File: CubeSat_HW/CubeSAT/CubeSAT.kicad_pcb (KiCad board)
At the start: 2 copper layers, 85 x 56 mm, 13 parts, among them J1 Conn_02x06_Odd_Even, J2 Conn_02x04_Odd_Even, J4 Conn_01x08_Pin, J5 Conn_01x06_Pin

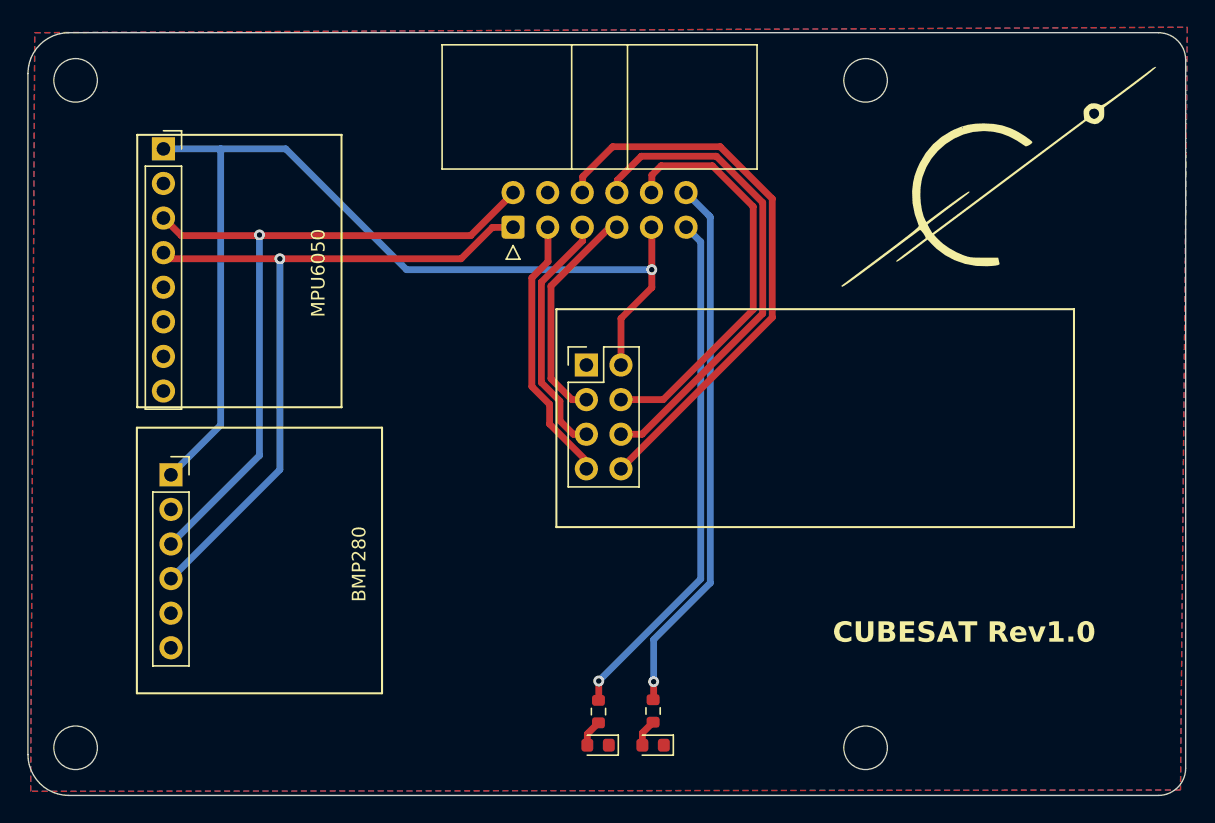
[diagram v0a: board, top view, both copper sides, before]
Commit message: Added version 2 of the PCB
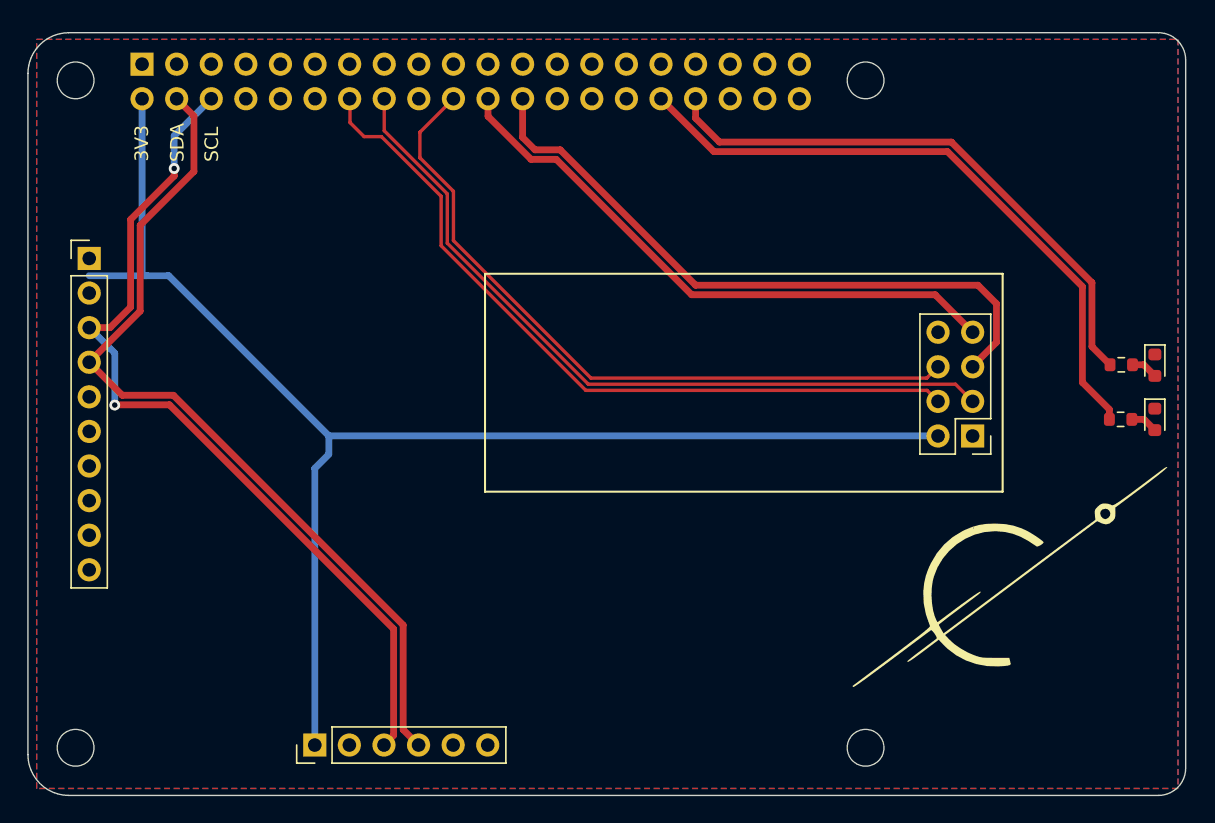
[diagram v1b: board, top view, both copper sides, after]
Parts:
- H1, H2, H3, H4: footprint MountingHole:MountingHole_3.2mm_M3 -> MountingHole:MountingHole_2.7mm
- J1: value Conn_02x06_Odd_Even -> Conn_01x10_Pin; footprint Connector_IDC:IDC-Header_2x06_P2.54mm_Horizontal -> Connector_PinHeader_2.54mm:PinHeader_1x10_P2.54mm_Vertical
- J4: value Conn_01x08_Pin -> Conn_02x20_Odd_Even; footprint Connector_PinSocket_2.54mm:PinSocket_1x08_P2.54mm_Vertical -> Connector_PinHeader_2.54mm:PinHeader_2x20_P2.54mm_Vertical; moved to B.Cu
- J5: footprint Connector_PinSocket_2.54mm:PinSocket_1x06_P2.54mm_Vertical -> Connector_PinHeader_2.54mm:PinHeader_1x06_P2.54mm_Vertical
- moved D1 49.5 mm to (262.7, 84.4), turned to -90 degrees
- moved R1 46.1 mm to (260.3, 84.4), turned to 0 degrees
- moved D2 43.9 mm to (262.7, 88.4), turned to -90 degrees
- moved R2 40.5 mm to (260.2, 88.4), turned to 0 degrees
- moved J1 31.2 mm to (184.5, 76.6), turned to 0 degrees
- moved G*** 29.4 mm to (252.1, 101.4)
- moved J2 28.8 mm to (249.4, 89.6), turned to 180 degrees
- moved J5 22.5 mm to (201.1, 112.3), turned to 90 degrees
- moved J4 6.42 mm to (188.4, 62.3), turned to -90 degrees
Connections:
- J1 pad 1: /SDA -> +3.3V
- J1 pad 10: /CSN -> unconnected-(J1-Pin_10-Pad10)
- J1 pad 2: /SCL -> GND
- J1 pad 3: /MISO -> /SCL
- J1 pad 4: GND -> /SDA
- J1 pad 5: /SCK -> unconnected-(J1-Pin_5-Pad5)
- J1 pad 6: /IRQ -> unconnected-(J1-Pin_6-Pad6)
- J1 pad 7: /CE -> unconnected-(J1-Pin_7-Pad7)
- J1 pad 8: /MOSI -> unconnected-(J1-Pin_8-Pad8)
- J1 pad 9: +3.3V -> unconnected-(J1-Pin_9-Pad9)
- J2 pad 8: /IRQ -> unconnected-(J2-Pin_8-Pad8)
- J4 pad 1: +3.3V -> unconnected-(J4-Pin_1-Pad1)
- J4 pad 2: GND -> +3.3V
- J4 pad 3: /SCL -> unconnected-(J4-Pin_3-Pad3)
- J4 pad 5: unconnected-(J4-Pin_5-Pad5) -> GND
- J4 pad 6: unconnected-(J4-Pin_6-Pad6) -> /SCL
- J4 pad 7: unconnected-(J4-Pin_7-Pad7) -> /TXD
- J4 pad 8: unconnected-(J4-Pin_8-Pad8) -> /GPIO4
- R1 pad 1: Net-(J1-Pin_11) -> /LED_1
- R2 pad 1: Net-(J1-Pin_12) -> /LED_2
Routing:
- net /LED_2: track 0.00 -> 47.2 mm
- net /LED_1: track 0.00 -> 42.1 mm
- net /IRQ: track 42.0 -> 0.00 mm
- net Net-(J1-Pin_12): track 39.7 -> 0.00 mm, vias 1 -> 0
- net /CE: track 16.7 -> 55.9 mm
- net Net-(J1-Pin_11): track 38.3 -> 0.00 mm, vias 1 -> 0
- net /SCK: track 18.4 -> 48.2 mm
- net +3.3V: track 76.0 -> 103.7 mm, vias 1 -> 0
- net /CSN: track 30.3 -> 55.5 mm
- net /MISO: track 19.9 -> 43.6 mm
- net /MOSI: track 36.0 -> 52.6 mm
- net /SCL: track 53.0 -> 64.0 mm, vias 1 -> 2
- net /SDA: track 53.6 -> 63.4 mm, vias 1 -> 0
- net GND: track 0.00 -> 0.57 mm
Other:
- board text added: "3V3"
- board text added: "CUBESAT Rev2.0"
- board text added: "SCL"
- board text added: "SDA"
- board text removed: "BMP280"
- board text removed: "CUBESAT Rev1.0"
- board text removed: "MPU6050"

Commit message: feat: Added Power and Com PCB
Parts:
- removed G***: LOGO, Logo:Logo
- removed J5: Conn_01x06_Pin, Connector_PinHeader_2.54mm:PinHeader_1x06_P2.54mm_Vertical
- added D3: G_LED, LED_SMD:LED_0603_1608Metric, F.Cu at (186.9, 93.0)
- added D4: G_LED, LED_SMD:LED_0603_1608Metric, F.Cu at (186.9, 88.0)
- added D5: G_LED, LED_SMD:LED_0603_1608Metric, F.Cu at (186.9, 98.0)
- added R3: 100R, Resistor_SMD:R_0603_1608Metric, F.Cu at (189.3, 93.0)
- added R4: 100R, Resistor_SMD:R_0603_1608Metric, F.Cu at (189.3, 88.0)
- added R5: 100R, Resistor_SMD:R_0603_1608Metric, F.Cu at (189.3, 98.0)
- moved D1 76.1 mm to (186.9, 78.0), turned to 90 degrees
- moved D2 76.0 mm to (186.9, 83.0), turned to 90 degrees
- moved R1 71.3 mm to (189.3, 78.0), turned to 180 degrees
- moved R2 71.1 mm to (189.3, 83.0), turned to 180 degrees
- moved J1 39.6 mm to (201.1, 112.5), turned to 90 degrees
- moved J2 21.0 mm to (228.4, 91.8)
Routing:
- net /GPIO19: track 0.00 -> 77.3 mm, vias 0 -> 1
- net /GPIO4: track 0.00 -> 39.0 mm, vias 0 -> 1
- net /GPIO17: track 0.00 -> 34.2 mm, vias 0 -> 1
- net /LED_1: track 42.1 -> 60.2 mm, vias 0 -> 1
- net /MOSI: track 52.6 -> 36.4 mm, vias 0 -> 1
- net /SCK: track 48.2 -> 37.1 mm, vias 0 -> 2
- net /MISO: track 43.6 -> 33.9 mm, vias 0 -> 2
- net /CSN: track 55.5 -> 46.7 mm, vias 0 -> 1
- net +3.3V: track 103.7 -> 96.4 mm, vias 0 -> 3
- net /LED_2: track 47.2 -> 54.0 mm, vias 0 -> 1
- net /CE: track 55.9 -> 51.2 mm, vias 0 -> 2
- net /SCL: track 64.0 -> 60.4 mm
- net /SDA: track 63.4 -> 65.4 mm, vias 0 -> 2
- net Net-(D5-A): track 0.00 -> 1.91 mm
- net Net-(D4-A): track 0.00 -> 1.91 mm
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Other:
- board text added: "CUBESAT Rev3.0"
- board text added: "LED STATUS1"
- board text added: "LED STATUS2"
- board text added: "LED STATUS3"
- board text added: "LED STATUS4"
- board text added: "LED STATUS5"
- board text removed: "3V3"
- board text removed: "CUBESAT Rev2.0"
- board text removed: "SCL"
- board text removed: "SDA"

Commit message: feat: Added new version for HW Board
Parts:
- moved J4 0.09 mm to (188.4, 62.2)
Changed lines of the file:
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@@
   )
   (footprint "Connector_PinHeader_2.54mm:PinHeader_2x20_P2.54mm_Vertical" (layer "B.Cu")
-    (at 188.38 62.31 -90)
+    (at 188.375 62.225 -90)
     (descr "Through hole straight pin header, 2x20, 2.54mm pitch, double rows")
     (tags "Through hole pin header THT 2x20 2.54mm double row")

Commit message: feat: Added GBR, BOM, CPL files for the project
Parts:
- removed J4: Conn_02x20_Odd_Even, Connector_PinHeader_2.54mm:PinHeader_2x20_P2.54mm_Vertical
- added J3: Conn_02x17_Odd_Even, Connector_IDC:IDC-Header_2x17_P2.54mm_Horizontal, F.Cu at (192.2, 66.8)
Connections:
- R3 pad 1: /GPIO19 -> /LED5
- R4 pad 1: /GPIO17 -> /LED4
- R5 pad 1: /GPIO4 -> /LED3
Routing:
- net /GPIO19: track 77.3 -> 0.00 mm, vias 1 -> 0
- net /LED5: track 0.00 -> 64.0 mm, vias 0 -> 4
- net /LED3: track 0.00 -> 63.8 mm, vias 0 -> 2
- net /LED4: track 0.00 -> 56.4 mm, vias 0 -> 2
- net /GPIO4: track 39.0 -> 0.00 mm, vias 1 -> 0
- net /GPIO17: track 34.2 -> 0.00 mm, vias 1 -> 0
- net /LED_1: track 60.2 -> 38.8 mm, vias 1 -> 2
- net GND: track 0.00 -> 16.6 mm, vias 103 -> 102
- net /SCK: track 37.1 -> 48.3 mm
- net /MISO: track 33.9 -> 43.4 mm
- net /MOSI: track 36.4 -> 45.7 mm
- net +3.3V: track 96.4 -> 88.4 mm, vias 3 -> 2
- net /LED_2: track 54.0 -> 46.2 mm, vias 1 -> 2
- net /SCL: track 60.4 -> 54.5 mm
- net /SDA: track 65.4 -> 59.8 mm
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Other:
- board text added: "CUBESAT Rev4.0"
- board text added: "LED STATUS 1"
- board text added: "LED STATUS 2"
- board text added: "LED STATUS 3"
- board text added: "LED STATUS 4"
- board text added: "LED STATUS 5"
- board text removed: "CUBESAT Rev3.0"
- board text removed: "LED STATUS1"
- board text removed: "LED STATUS2"
- board text removed: "LED STATUS3"
- board text removed: "LED STATUS4"
- board text removed: "LED STATUS5"

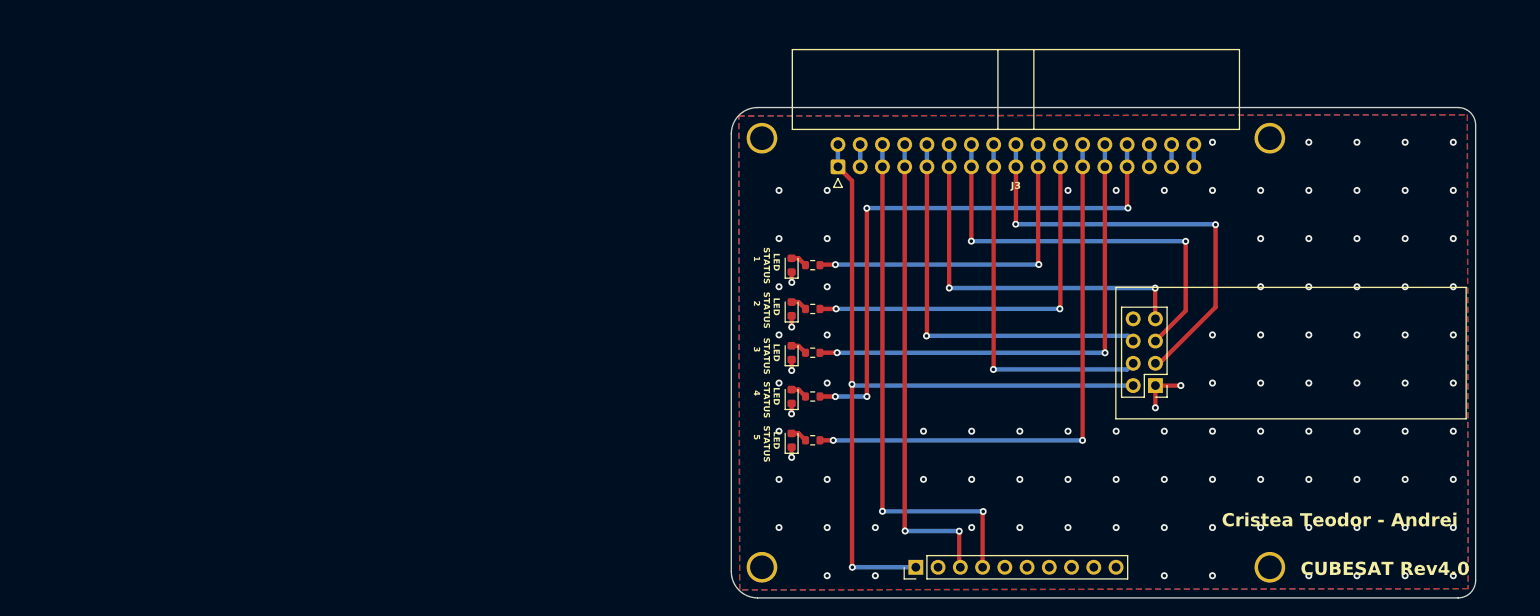
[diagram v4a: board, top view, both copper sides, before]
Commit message: feat: Added Payload Board and new Gerbers for the project
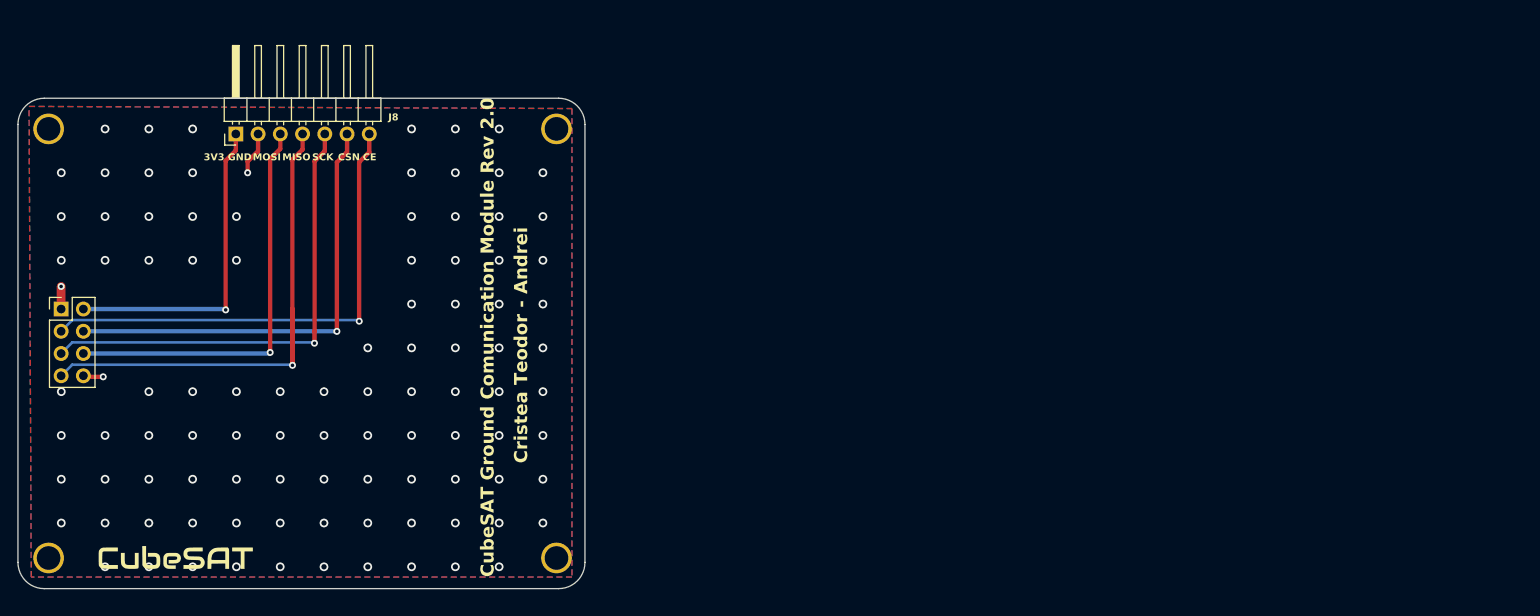
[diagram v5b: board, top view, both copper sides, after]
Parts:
- removed D1, D2, D3, D4, D5: G_LED, LED_SMD:LED_0603_1608Metric
- removed J1: Conn_01x10_Pin, Connector_PinHeader_2.54mm:PinHeader_1x10_P2.54mm_Vertical
- removed J3: Conn_02x17_Odd_Even, Connector_IDC:IDC-Header_2x17_P2.54mm_Horizontal
- removed R1, R2, R3, R4, R5: 100R, Resistor_SMD:R_0603_1608Metric
- added G***: LOGO, Logo:Logo, F.Cu at (116.6, 111.3)
- added J8: Conn_01x07_Pin, Connector_PinHeader_2.54mm:PinHeader_1x07_P2.54mm_Horizontal, F.Cu at (123.4, 63.0)
- moved J2 125.3 mm to (103.5, 83.0), turned to 0 degrees
- moved H1 81.5 mm to (102.0, 62.4)
- moved H2 81.5 mm to (160.0, 62.4)
- moved H3 81.5 mm to (160.0, 111.4)
- moved H4 81.5 mm to (102.0, 111.4)
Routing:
- net /LED5: track 64.0 -> 0.00 mm, vias 4 -> 0
- net /LED3: track 63.8 -> 0.00 mm, vias 2 -> 0
- net /SDA: track 59.8 -> 0.00 mm, vias 2 -> 0
- net /LED4: track 56.4 -> 0.00 mm, vias 2 -> 0
- net /SCL: track 54.5 -> 0.00 mm, vias 2 -> 0
- net +3.3V: track 88.4 -> 37.0 mm, vias 2 -> 1
- net /LED_2: track 46.2 -> 0.00 mm, vias 2 -> 0
- net /LED_1: track 38.8 -> 0.00 mm, vias 2 -> 0
- net /MISO: track 43.4 -> 60.4 mm, vias 2 -> 1
- net /CSN: track 41.9 -> 52.0 mm
- net GND: track 16.6 -> 7.50 mm, vias 102 -> 100
- net /CE: track 50.9 -> 56.5 mm, vias 2 -> 1
- net /SCK: track 48.3 -> 53.9 mm, vias 2 -> 1
- net /PWM1: track 2.54 -> 0.00 mm
- net /PWM0: track 2.54 -> 0.00 mm
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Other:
- board size 85 x 56 mm -> 64.8 x 56 mm
- board text added: "3V3"
- board text added: "CE"
- board text added: "CSN"
- board text added: "CubeSAT Ground Comunication Module Rev 2.0"
- board text added: "GND"
- board text added: "MISO"
- board text added: "MOSI"
- board text added: "SCK"
- board text removed: "CUBESAT Rev4.0"
- board text removed: "LED STATUS 1"
- board text removed: "LED STATUS 2"
- board text removed: "LED STATUS 3"
- board text removed: "LED STATUS 4"
- board text removed: "LED STATUS 5"
